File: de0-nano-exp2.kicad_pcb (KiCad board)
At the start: 2 copper layers, 68.6 x 61 mm, 16 parts, among them J1 Conn_01x03, J2 DE0_Nano_GPIO1, J3 USB_B_Micro, J4 PIDP11_HDR, J5 PMODNIC100, U1 CP2102

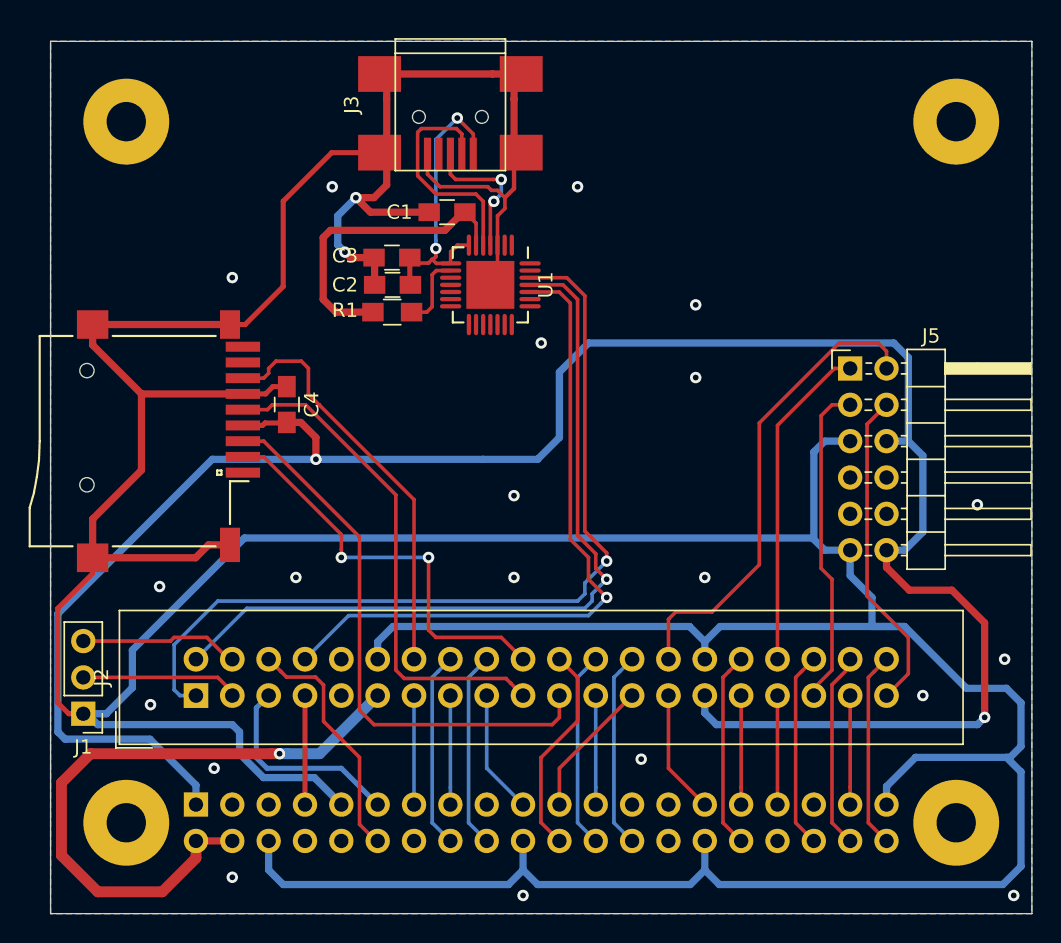
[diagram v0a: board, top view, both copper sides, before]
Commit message: fix wrong pin layout for pmod connector
plus other smaller tweaks
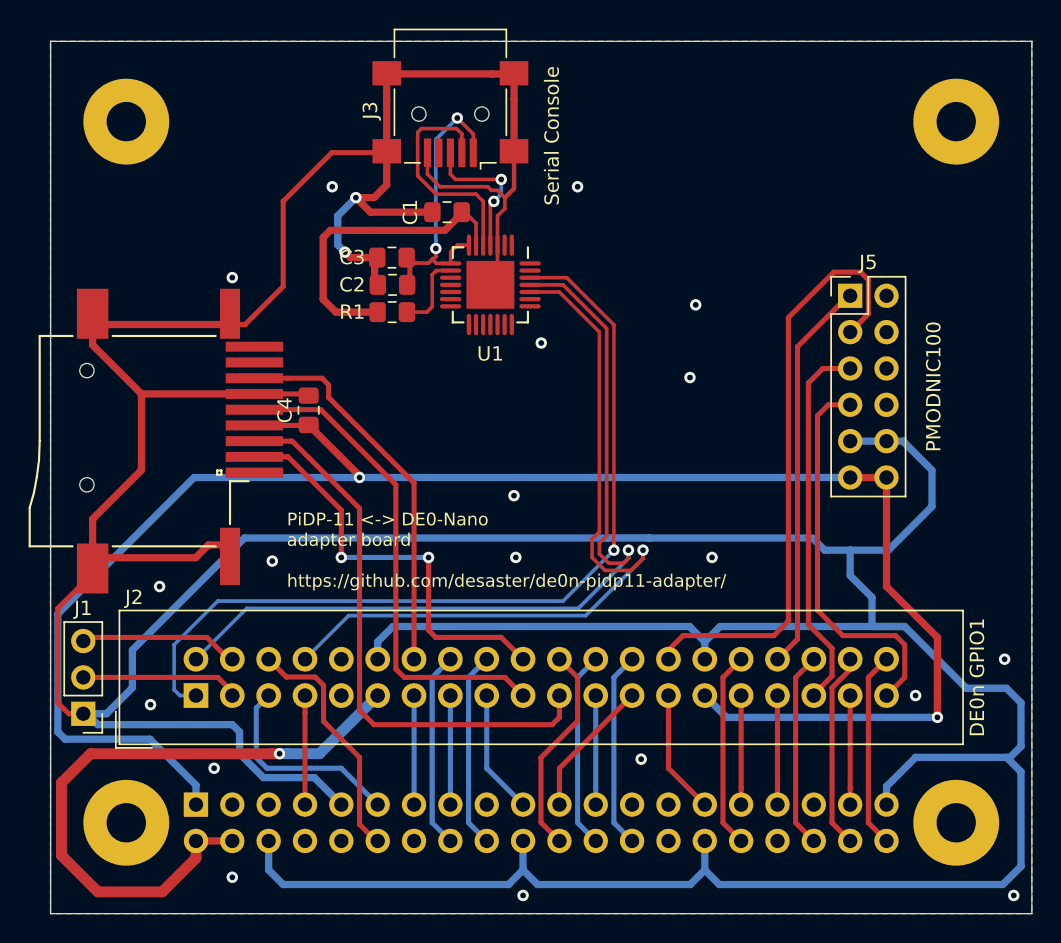
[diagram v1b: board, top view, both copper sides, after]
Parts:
- removed REF** (x4): MountingHole_raspi, Mounting_Holes:MountingHole_2.7mm_Pad
- added H1: MountingHole, MountingHole_RasPI:MountingHole_RasPI, F.Cu at (137.4, 71.7)
- added H2: MountingHole, MountingHole_RasPI:MountingHole_RasPI, F.Cu at (195.4, 120.7)
- added H3: MountingHole, MountingHole_RasPI:MountingHole_RasPI, F.Cu at (195.4, 71.7)
- added H4: MountingHole, MountingHole_RasPI:MountingHole_RasPI, F.Cu at (137.4, 120.7)
- C1, C2, C3, C4: footprint Capacitors_SMD:C_0805_HandSoldering -> Capacitor_SMD:C_0805_2012Metric_Pad1.15x1.40mm_HandSolder
- J1: footprint Pin_Headers:Pin_Header_Straight_1x03_Pitch2.54mm -> Connector_PinHeader_2.54mm:PinHeader_1x03_P2.54mm_Vertical
- J2: footprint Connectors_IDC:IDC-Header_2x20_Pitch2.54mm_Straight -> Connector_IDC:IDC-Header_2x20_P2.54mm_Vertical
- J3: footprint Connectors:USB_Mini-B -> Connector_USB:USB_Mini-B_Lumberg_2486_01_Horizontal
- J4: footprint Pin_Headers:Pin_Header_Straight_2x20_Pitch2.54mm -> Connector_PinHeader_2.54mm:PinHeader_2x20_P2.54mm_Vertical
- J5: footprint Pin_Headers:Pin_Header_Angled_2x06_Pitch2.54mm -> pmodnic:pmodnic
- R1: footprint Resistors_SMD:R_0805_HandSoldering -> Resistor_SMD:R_0805_2012Metric_Pad1.15x1.40mm_HandSolder
- moved J5 5.08 mm to (188.0, 83.8)
- moved C4 1.58 mm to (150.1, 91.8)
- turned J3 to 180 degrees
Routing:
- net +3V3: track 153.5 -> 128.5 mm
- net /DE0_N16: track 33.3 -> 42.4 mm
- net GND: track 370.8 -> 378.1 mm, vias 23 -> 21
- net /DE0_T12: track 47.6 -> 53.9 mm
- net /DE0_J13: track 22.7 -> 27.4 mm
- net /DE0_N14: track 23.1 -> 27.6 mm
- net /DE0_F13: track 55.5 -> 59.3 mm
- net /DE0_M10: track 22.7 -> 26.4 mm
- net /DE0_L16: track 39.1 -> 41.0 mm
- net /DE0_R11: track 28.9 -> 27.2 mm
- net /DE0_N11: track 29.4 -> 31.0 mm
- net /DE0_N9: track 35.7 -> 34.6 mm
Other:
- board text added: "DE0n GPIO1"
- board text added: "PMODNIC100"
- board text added: "PiDP-11 <-> DE0-Nano adapter board https://github.com/desaster/de0n-pidp11-adapter/"
- board text added: "PiDP-11 Connector"
- board text added: "Serial Console"
